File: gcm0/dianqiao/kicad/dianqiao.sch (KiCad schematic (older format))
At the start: 65 parts, among them U2 LM2596T-ADJ, U3 LM1117-3.3, U5 STM32F030F4P6, Y1 Crystal

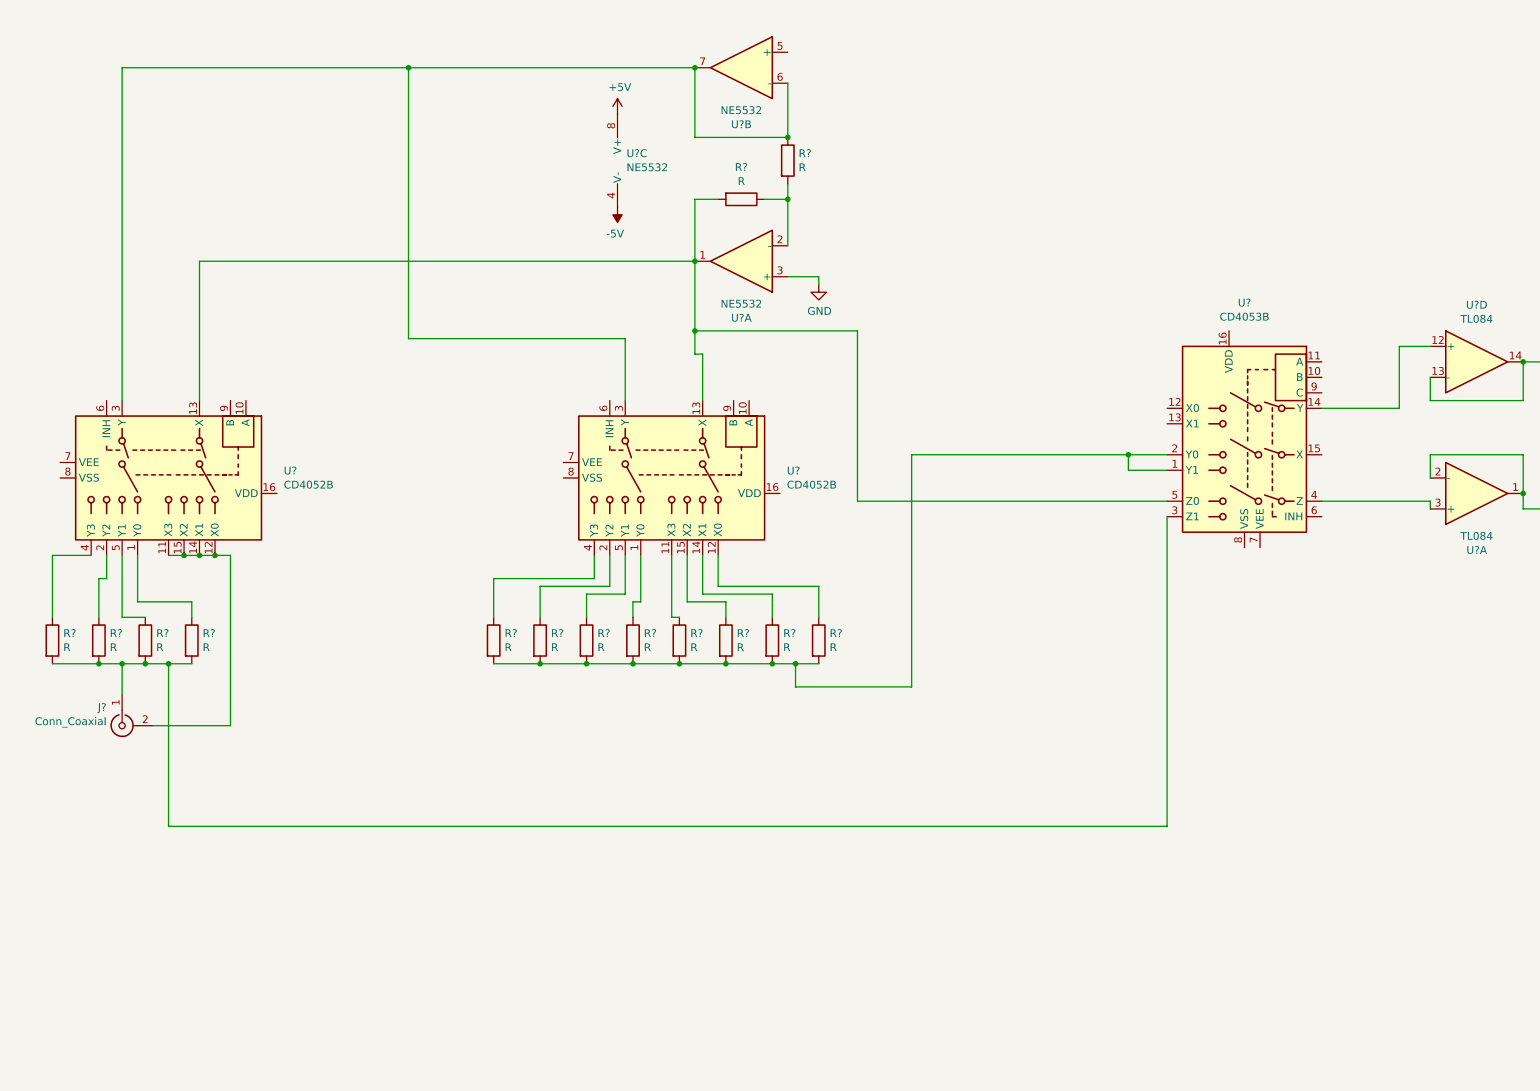
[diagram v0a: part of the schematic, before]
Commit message: adc采样和DFT
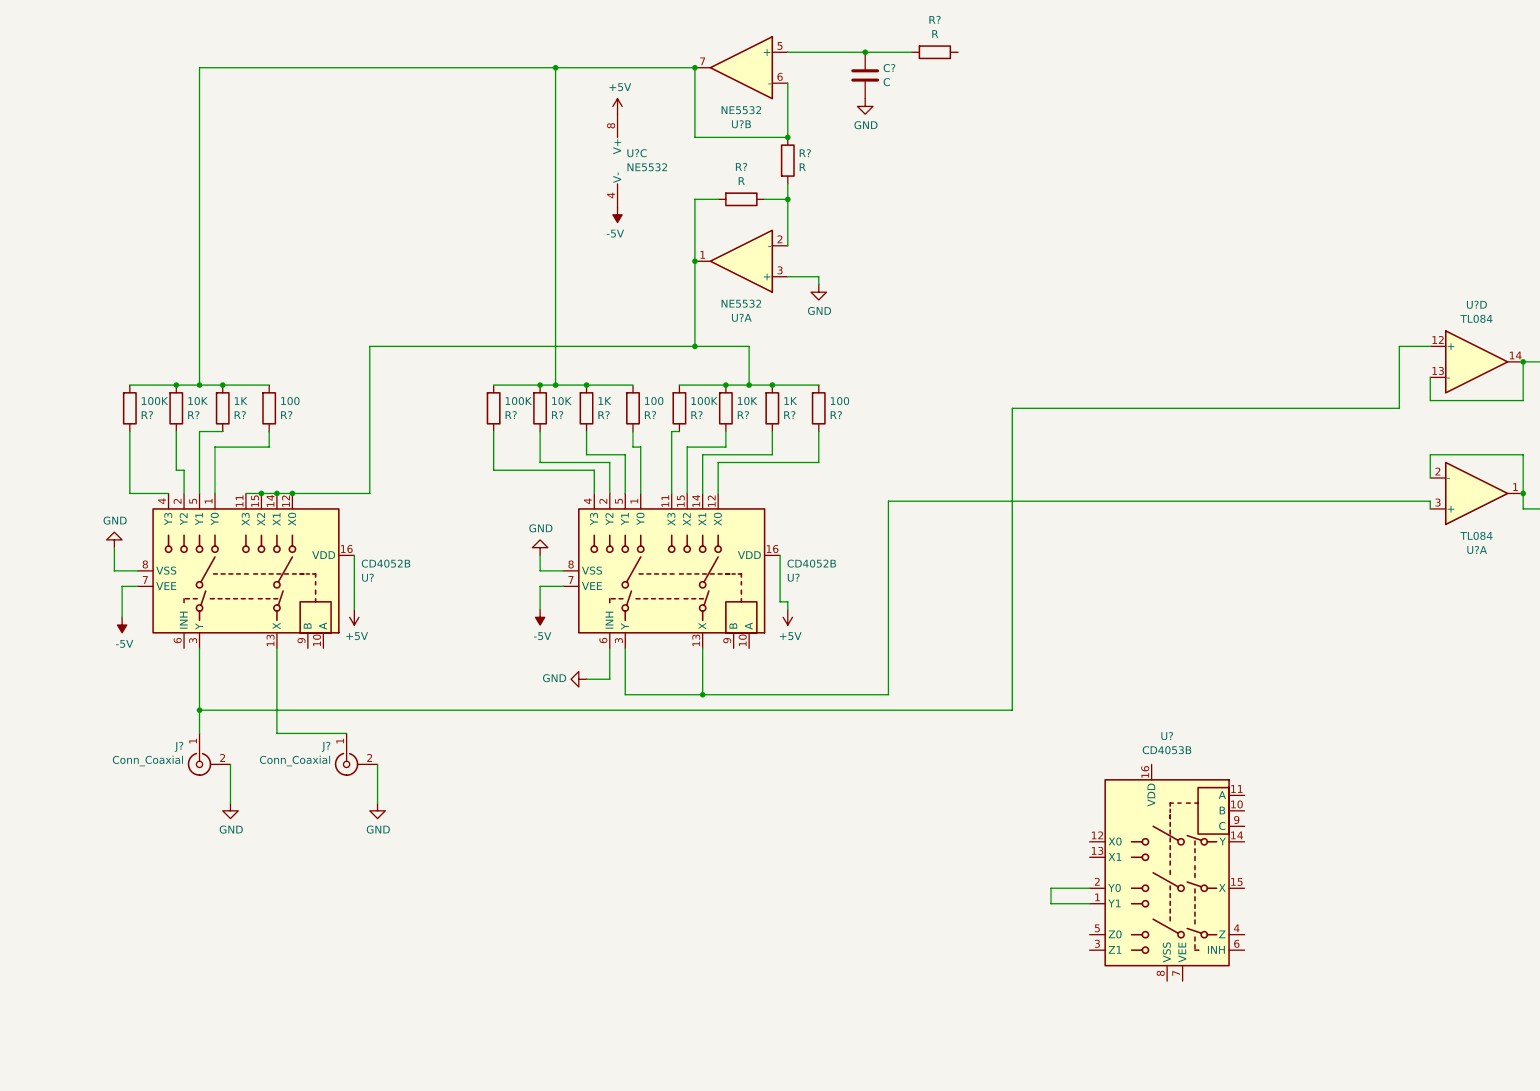
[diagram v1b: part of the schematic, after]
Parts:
- added C?: C, symbol Device:C
- added J?: Conn_Coaxial, symbol Connector:Conn_Coaxial
- added R?: R, symbol Device:R
- R? (x3): value R -> 100K
- R? (x3): value R -> 10K
- R? (x3): value R -> 1K
- R? (x3): value R -> 100
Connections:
- net +5V: now also U?.16 (VDD), U?.16 (VDD)
- net -5V: now also U?.7 (VEE), U?.7 (VEE)
- net GND: now also J?.2 (Ext), U?.6 (INH), U?.8 (VSS), U?.8 (VSS), C?.2, J?.2 (Ext)
- net at U?.11 (X3), U?.12 (X0), U?.14 (X1)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: now also R?.2, R?.2, R?.2, R?.2, R?.2, U?.1; no longer J?.2 (Ext)
- net at R?.1, U?.6 (-), U?.7: now also R?.2, R?.2, R?.2, R?.2, R?.2, R?.2, R?.2, R?.2; no longer U?.3 (Y), U?.3 (Y)
- net at U?.5 (+): now also C?.1, R?.2
- net at U?.3 (+): now also U?.13 (X), U?.3 (Y); no longer U?.4 (Z)
- net at U?.12 (+): now also J?.1 (In), U?.3 (Y); no longer U?.14 (Y)
- new net: J?.1 (In), U?.13 (X)
- new net: U?.1 (Y1), U?.2 (Y0)
- now unconnected: U?.3 (Z1), U?.5 (Z0)
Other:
- moved on the sheet: J?, R?, U?

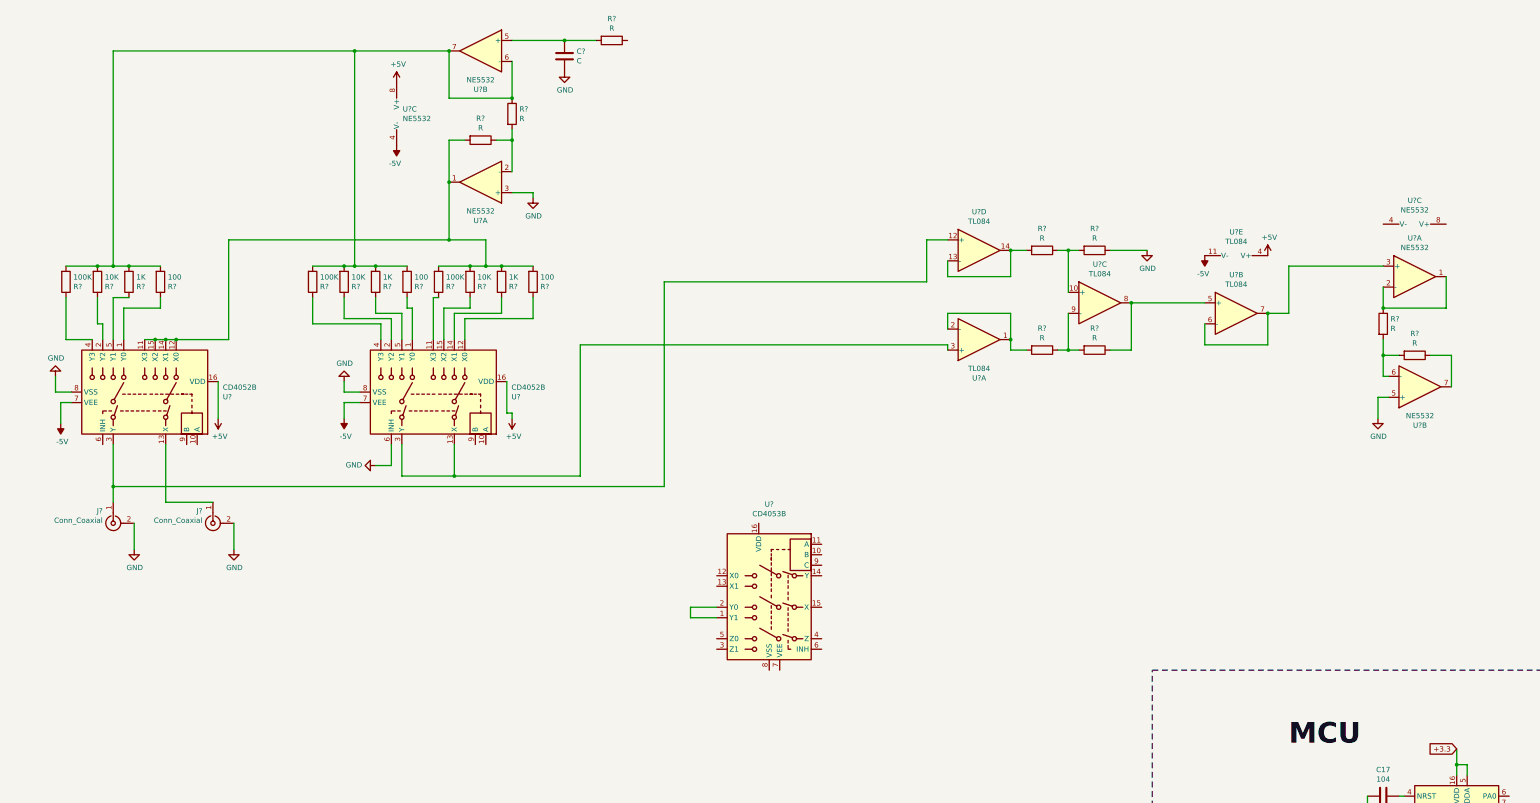
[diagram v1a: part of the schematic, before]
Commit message: 改电路改方案
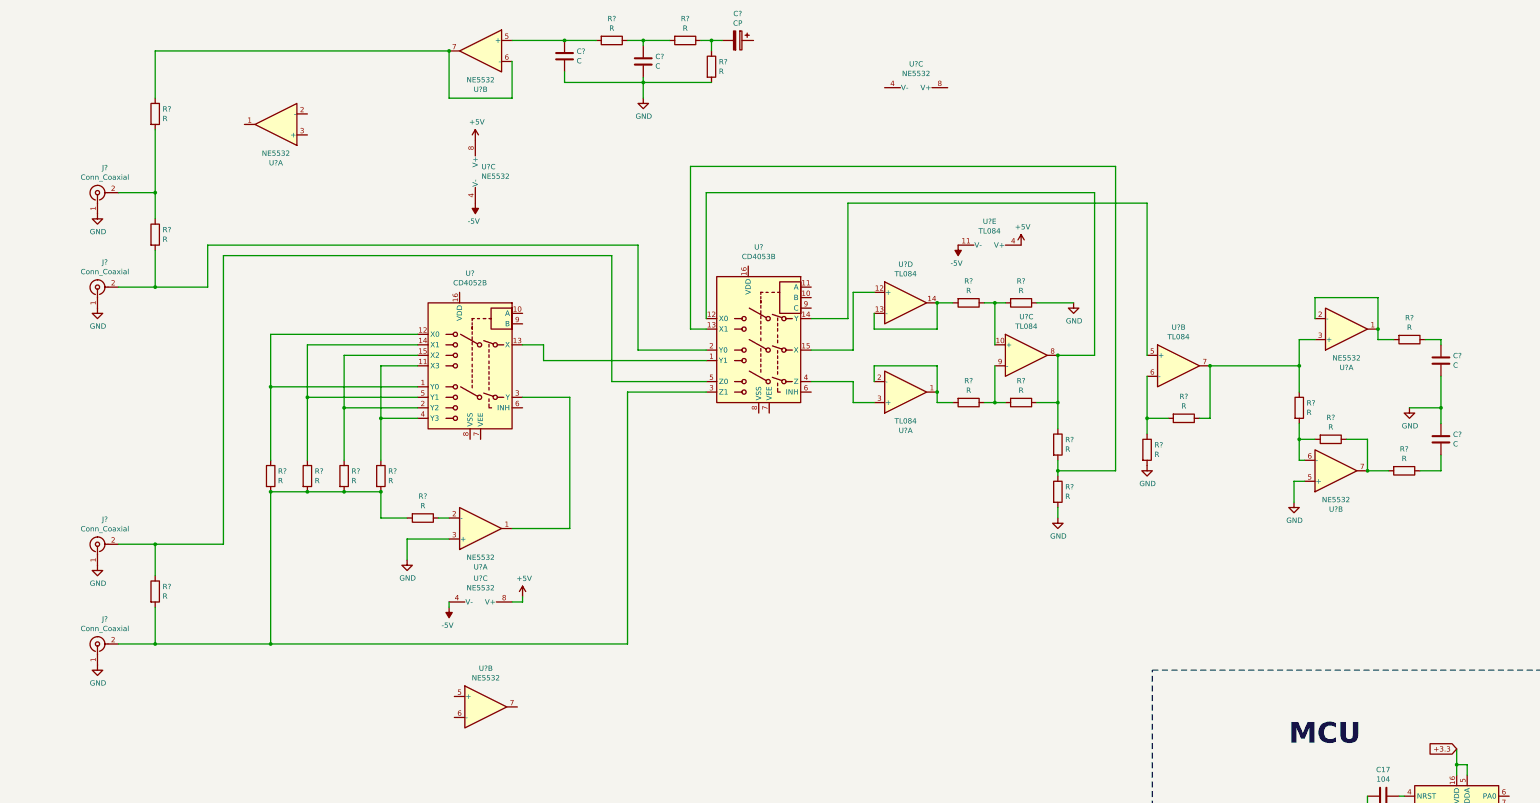
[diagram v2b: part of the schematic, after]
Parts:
- removed J? (x2): Conn_Coaxial, symbol Connector:Conn_Coaxial
- removed R? (x3): 100K, symbol Device:R
- removed R? (x3): 10K, symbol Device:R
- removed R? (x3): 1K, symbol Device:R
- removed R? (x3): 100, symbol Device:R
- removed R? (x2): R, symbol Device:R
- removed U? (x2): CD4052B, symbol Analog_Switch:CD4052B
- removed U?: CD4053B, symbol Analog_Switch:CD4053B
- added C? (x3): C, symbol Device:C
- added C?: CP, symbol Device:CP
- added J? (x4): Conn_Coaxial, symbol Connector:Conn_Coaxial
- added R? (x16): R, symbol Device:R
- added U?: CD4053B, symbol Analog_Switch:CD4053B
- added U? (x3): NE5532, symbol Amplifier_Operational:NE5532
- added U?: CD4052B, symbol Analog_Switch:CD4052B
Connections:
- net +5V: now also U?.8 (V+)
- net -5V: now also U?.4 (V-)
- net GND: now also C?.1, C?.2, C?.2, J?.1 (In), J?.1 (In), J?.1 (In), J?.1 (In), R?.2, R?.2, R?.2, U?.3 (+); no longer U?.3 (+)
- net at R?.1: now also C?.1, R?.2
- net at U?.12 (+): now also U?.15 (X)
- net at U?.3 (+): now also U?.4 (Z)
- net at U?.6 (-), U?.7: now also R?.1
- net at R?.1, U?.8: now also R?.1, U?.12 (X0); no longer U?.5 (+)
- net at U?.3 (+), U?.7: now also R?.1, R?.1; no longer U?.6 (-)
- net at U?.1, U?.2 (-): now also R?.2; no longer R?.1
- net at R?.1, U?.7: now also R?.2
- new net: U?.1 (Y1), U?.13 (X)
- new net: R?.1, R?.2, U?.13 (X1)
- new net: U?.14 (Y), U?.5 (+)
- new net: J?.2 (Ext), R?.2, U?.2 (Y0)
- new net: J?.2 (Ext), R?.2, R?.2, R?.2, R?.2, R?.2, R?.2, U?.3 (Z1)
- new net: J?.2 (Ext), R?.1, U?.5 (Z0)
- new net: C?.2, R?.1, R?.1
- new net: U?.1, U?.3 (Y)
- new net: R?.1, U?.2 (-)
- new net: J?.2 (Ext), R?.1, R?.2
- new net: R?.1, U?.1 (Y0), U?.12 (X0)
- new net: R?.1, U?.11 (X3), U?.4 (Y3)
- new net: R?.1, U?.14 (X1), U?.5 (Y1)
- new net: R?.1, U?.15 (X2), U?.2 (Y2)
- new net: R?.1, R?.2, U?.6 (-)
- new net: C?.1, R?.1
- new net: C?.2, R?.1
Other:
- moved on the sheet: R?, U?A, U?B, U?C, U?D, U?E

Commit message: 自动平衡桥方案失败
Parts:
- removed C? (x2): C, symbol Device:C
- removed R? (x8): R, symbol Device:R
- added C16, C18: 102, symbol Device:C
- added R18: 10K, symbol Device:R
- added R21, R24, R28: R, symbol Device:R
- added R25, R26, R31, R35: 1K, symbol Device:R
- added R30: 5K, symbol Device:R
- added R32, R33: 20K, symbol Device:R
- added R34: 7K, symbol Device:R
- added R36, R37: 500, symbol Device:R
- added SW1, SW2: SW_Push, symbol Switch:SW_Push
- added U11: CD4053B, symbol Analog_Switch:CD4053B
- C11, C12: renamed from C?; value C -> 102
- C15: renamed from C?; value CP -> 4.7uF
- R10, R3, R4, R5, R6, R9: renamed from R?; value R -> 100
- R11, R13: renamed from R?; value R -> 500
- R16: renamed from R?; value R -> 100K
- R19, R20, R22, R23, R7: renamed from R?; value R -> 1K
- R8: renamed from R?; value R -> 10K
- Y1: value Crystal -> 8M
- gave numbers to parts that had none: 18
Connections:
- net +5V: now also U12.8 (V+), U6.16 (VDD), U8.16 (VDD), R18.1, R21.1, R24.1, R28.1, U11.16 (VDD)
- net -5V: now also U12.4 (V-), U6.7 (VEE), U8.7 (VEE), U11.7 (VEE)
- net GND: now also U6.6 (INH), U6.8 (VSS), U8.6 (INH), U8.8 (VSS), C16.2, C18.2, R26.2, R31.2, R35.2, SW1.1, SW2.2, U11.6 (INH), U11.8 (VSS)
- net PA4: now reaches U5.10 (PA4)
- net PA4: now also R21.2, U11.11 (A)
- net at U5.14 (PB1): now also SW1.2
- net PA9: now reaches U5.17 (PA9)
- net PA9: now also U8.10 (B), U8.11 (A), U8.9 (C), R18.2
- net at U5.18 (PA10): now also SW2.1
- net ADC1: now reaches U5.6 (PA0)
- net ADC1: now also C18.1, R36.1
- net ADC2: now reaches U5.7 (PA1)
- net ADC2: now also C16.1, R37.1
- net PA2: now reaches U5.8 (PA2)
- net PA2: now also R28.2, U11.9 (C)
- net PA3: now reaches U5.9 (PA3)
- net PA3: now also R24.2, U11.10 (B)
- net liang_cheng: now reaches U9.6 (QG)
- net liang_cheng: now also U6.9 (B)
- net liang_cheng1: now reaches U9.7 (QH)
- net liang_cheng1: now also U6.10 (A)
- net at R23.1, U10.8: now also R25.1, U11.13 (X1); no longer U8.12 (X0)
- net at U8.14 (Y): no longer U10.5 (+)
- net at U10.6 (-): now also U11.15 (X)
- net at U10.7, U12.3 (+): now also R30.1, U11.1 (Y1)
- net at U12.1: now also R32.2, R34.1, R37.2, U11.3 (Z1); no longer U12.2 (-)
- net at U12.6 (-): now also R32.1, R33.2
- net at U12.7: now also R33.1, R36.2
- net +12 renamed +9V
- new net: U10.5 (+), U11.14 (Y)
- new net: U11.4 (Z), U12.2 (-)
- new net: R25.2, R26.1, U11.12 (X0)
- new net: R30.2, R31.1, U11.2 (Y0)
- new net: R34.2, R35.1, U11.5 (Z0)
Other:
- moved on the sheet: U10B, U12A, U12B, U12C

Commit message: 显示阻抗
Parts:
- removed unit 3 of U1
- removed U11: CD4053B, symbol Analog_Switch:CD4053B
- removed unit 1 of U7
- removed unit 2 of U7
- added C19, C20: 102, symbol Device:C
- added SW3: 1, symbol Switch:SW_Push
- added U11: NE5532, symbol Amplifier_Operational:NE5532
- C3: value 100uF -> 1000uF
- R10: value 100 -> 10K
- R11, R13: value 500 -> 1K
- R19, R20: value 1K -> 500
- R21: value R -> 9K
- R24: value R -> 1K
- R26: value 1K -> 9K
- R28: value R -> 100
- R30: value 5K -> 1K
- R34: value 7K -> 10K
- R35: value 1K -> 5K
- R36, R37: value 500 -> 100
- R9: value 100 -> 100K
- SW1: value SW_Push -> 2
- SW2: value SW_Push -> 0
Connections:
- net +5V: now also R10.2, R18.2, U11.8 (V+); no longer R18.1, R21.1, R24.1, R28.1
- net -5V: now also U11.4 (V-)
- net GND: now also R24.2, R25.2, C19.2, C20.2, SW3.2, U11.3 (+); no longer R26.2, R31.2
- net PA3: now also R18.1, U8.11 (A); no longer R24.2
- net PA9: now also R10.1; no longer R18.2, U8.11 (A)
- net at SW2.1: now also U5.8 (PA2); no longer U5.18 (PA10)
- net at U5.2 (PF0), Y1.2: now also C13.1
- net at U8.12 (X0): now also R21.2, R24.1
- net at U8.13 (X1): now also R21.1, R23.1, U10.8
- net at U8.14 (Y): now also U10.5 (+)
- net at J4.2 (Ext), R5.2, R6.2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: now also R28.1; no longer R10.2
- net SPWM: now reaches C15.1
- net SPWM: now also U5.18 (PA10)
- net at U6.3 (Y): now also U11.1
- net at U1.1: now also R3.1, U1.2 (-)
- net at U1.3 (+): now also R30.2, C19.1
- net at U10.6 (-): now also R25.1, R26.2
- net at U10.7, U12.3 (+): now also R26.1; no longer R30.1
- net at R32.2, R37.2, U12.1: now also U12.2 (-); no longer R34.1
- net at R31.1: now also R34.1, U1.7; no longer R30.2
- net at R34.2, R35.1: now also U1.6 (-)
- net PA2: no longer names the net of R28.2
- net PA2: now also U11.2 (-); no longer U5.8 (PA2)
- net PA4: no longer names the net of U5.10 (PA4)
- net PA4: now also SW3.1; no longer R21.2
- new net: C20.1, R30.1, R31.2
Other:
- moved on the sheet: U10B, U1A, U7C

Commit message: 频率切换
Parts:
- removed R34: 10K, symbol Device:R
- removed R35: 5K, symbol Device:R
- added C21: 101, symbol Device:C
- added R38: 20k, symbol Device:R
- added R39: 10k, symbol Device:R
- added R40: 10K, symbol Device:R
- C11, C12: value 102 -> 101
- C19: value 102 -> 68
- C20: value 102 -> 331
- R11, R13: value 1K -> 10K
- R19, R20: value 500 -> 1K
- R30: value 1K -> 20k
- R31: value 1K -> 100k
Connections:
- net GND: now also C21.2; no longer C20.2
- net at C15.2, R16.1: now also R40.1; no longer R13.1
- net at U1.7: now also U1.6 (-), R38.1, R39.1; no longer R31.1
- net at R3.1, U1.1, U1.2 (-): now also C20.1
- net at C19.1, R30.2, U1.3 (+): now also R31.2
- new net: C21.1, R13.1, R40.2
- new net: C20.2, R30.1, R31.1, R38.2, R39.2
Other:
- moved on the sheet: C15, R16

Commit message: 频率切换成功
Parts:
- added R?: 10K, symbol Device:R
- added R?: 20K, symbol Device:R
- added R?: 100K, symbol Device:R
- R3: value 100 -> 200
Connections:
- net GND: now also R?.2, R?.2
- net at R38.1, R39.1, U1.7: now also R?.1; no longer U1.6 (-)
- new net: R?.1, R?.1, R?.2, U1.6 (-)
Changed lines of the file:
@@
 Wire Wire Line
 	7300 1950 7300 3550
-Connection ~ 4850 1000
 Wire Wire Line
 	2700 1200 2700 1400
@@
 P 1950 1750
 F 0 "R3" H 2020 1796 50  0000 L CNN
-F 1 "100" H 2020 1705 50  0000 L CNN
+F 1 "200" H 2020 1705 50  0000 L CNN
 F 2 "" V 1880 1750 50  0001 C CNN
 F 3 "~" H 1950 1750 50  0001 C CNN
@@
 	1    0    0    -1
 $EndComp
-Wire Wire Line
-	5450 1100 5450 1850
 $Comp
 L Device:R R40
@@
 Wire Wire Line
 	3000 1200 3000 1700
-Wire Wire Line
-	5450 1850 4850 1850
-Wire Wire Line
-	4850 1000 4850 1850
+$Comp
+L Device:R R?
+U 1 1 5F481BA7
+P 4850 1600
+F 0 "R?" H 4920 1646 50  0000 L CNN
+F 1 "10K" H 4920 1555 50  0000 L CNN
+F 2 "" V 4780 1600 50  0001 C CNN
+F 3 "~" H 4850 1600 50  0001 C CNN
+	1    4850 1600
+	1    0    0    -1
+$EndComp
+$Comp
+L Device:R R?
+U 1 1 5F48359F
+P 4850 2100
+F 0 "R?" H 4920 2146 50  0000 L CNN
+F 1 "20K" H 4920 2055 50  0000 L CNN
+F 2 "" V 4780 2100 50  0001 C CNN
+F 3 "~" H 4850 2100 50  0001 C CNN
+	1    4850 2100
+	1    0    0    -1
+$EndComp
+$Comp
+L Device:R R?
+U 1 1 5F484BA7
+P 5250 2100
+F 0 "R?" H 5320 2146 50  0000 L CNN
+F 1 "100K" H 5320 2055 50  0000 L CNN
+F 2 "" V 5180 2100 50  0001 C CNN
+F 3 "~" H 5250 2100 50  0001 C CNN
+	1    5250 2100
+	1    0    0    -1
+$EndComp
+Wire Wire Line
+	5250 1950 4850 1950
+Wire Wire Line
+	4850 1750 4850 1950
+Connection ~ 4850 1950
+Wire Wire Line
+	4850 1450 4850 1000
+Connection ~ 4850 1000
+Wire Wire Line
+	5250 2250 5000 2250
+$Comp
+L power:GND #PWR?
+U 1 1 5F51CD3A
+P 5000 2400
+F 0 "#PWR?" H 5000 2150 50  0001 C CNN
+F 1 "GND" H 5005 2227 50  0000 C CNN
+F 2 "" H 5000 2400 50  0001 C CNN
+F 3 "" H 5000 2400 50  0001 C CNN
+	1    5000 2400
+	1    0    0    -1
+$EndComp
+Wire Wire Line
+	5000 2400 5000 2250
+Connection ~ 5000 2250
+Wire Wire Line
+	5000 2250 4850 2250
+Wire Wire Line
+	5450 1100 5450 1950
+Wire Wire Line
+	5450 1950 5250 1950
+Connection ~ 5250 1950
 $EndSCHEMATC
